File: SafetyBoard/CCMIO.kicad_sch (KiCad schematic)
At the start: 24 parts, among them J13 RTD B, J14 Brakelight, J15 SHOCK/WHEEL SNSR, J16 footwell, J18 AMP, J19 39306207

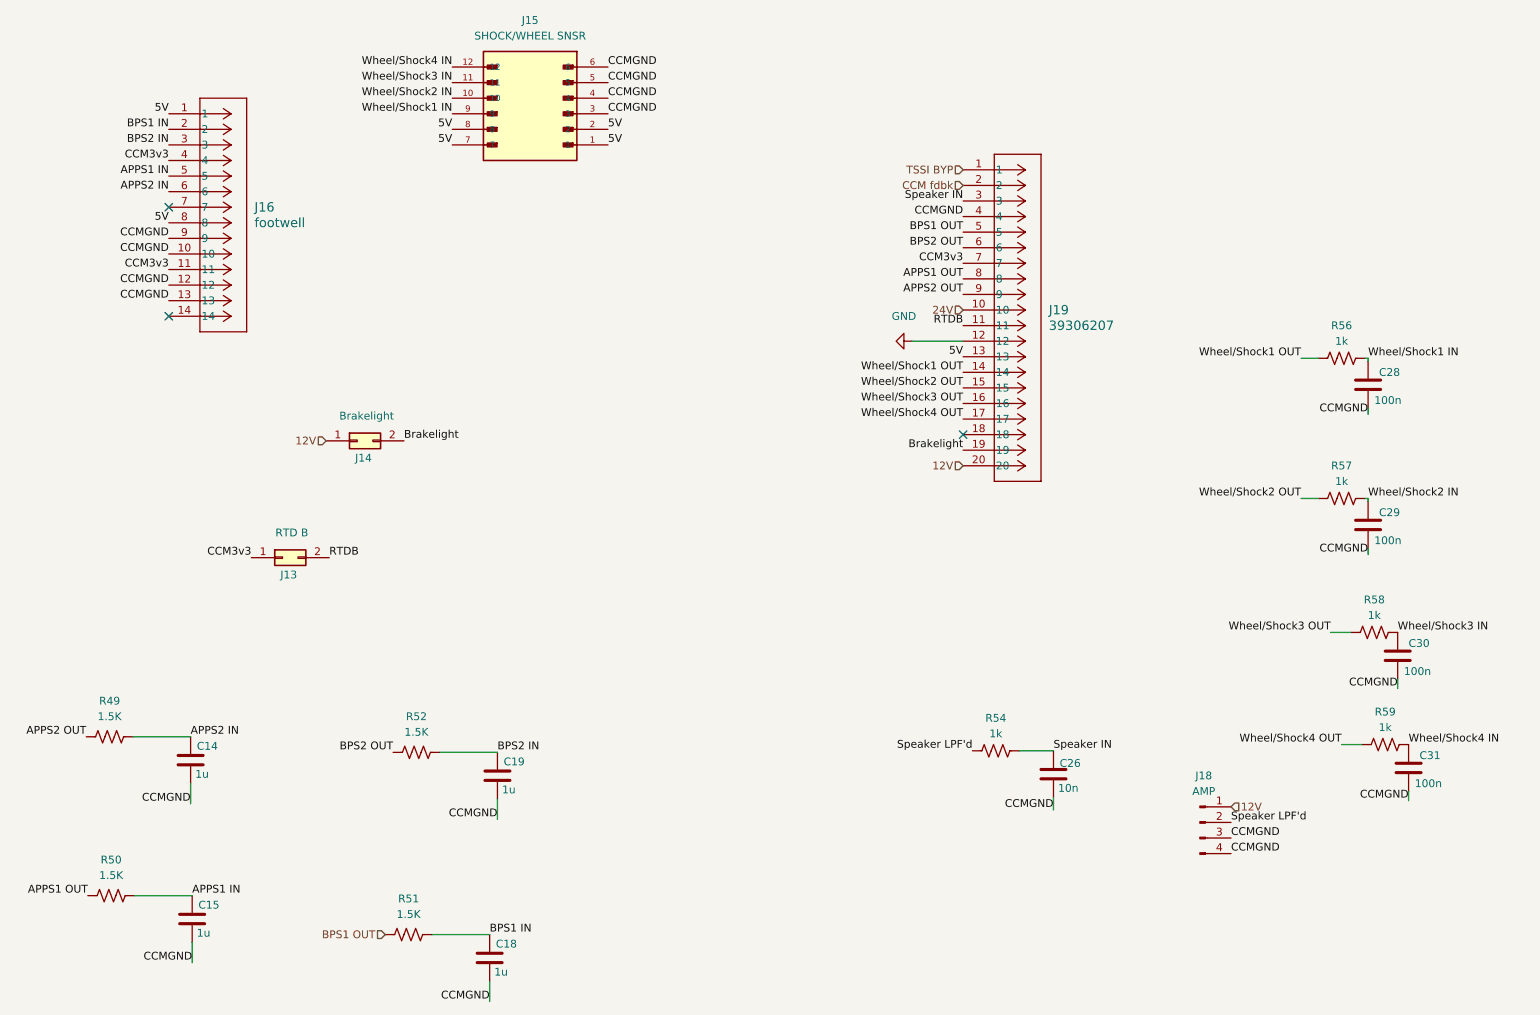
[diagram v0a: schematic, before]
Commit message: I think think this is final but need to defuck the BOM
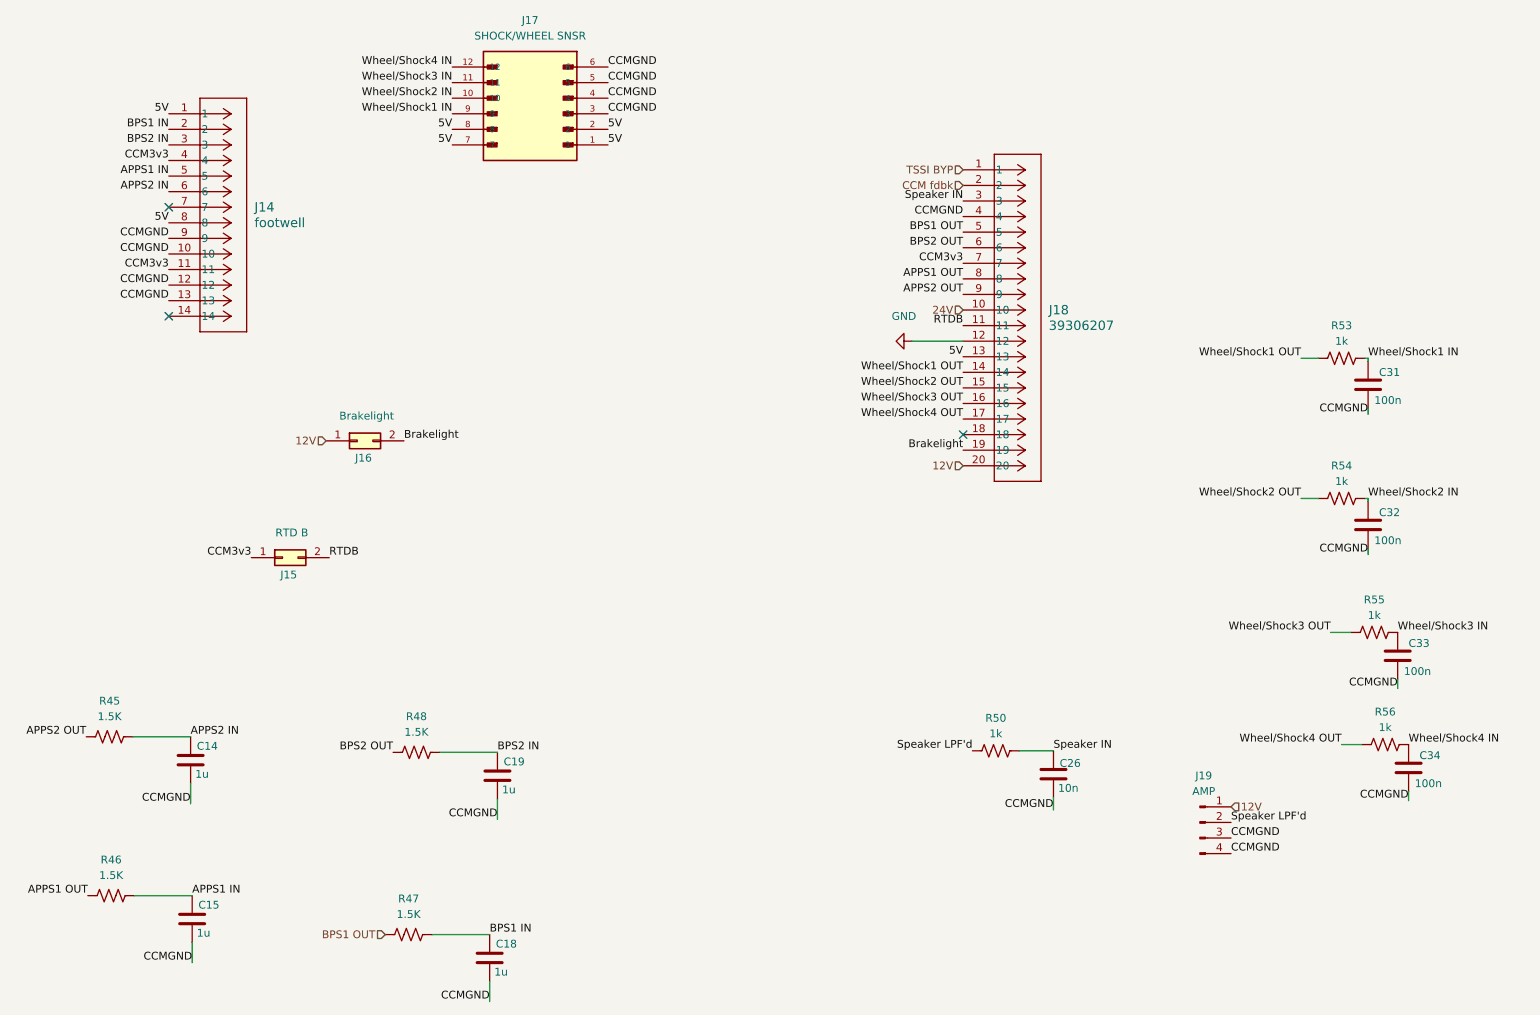
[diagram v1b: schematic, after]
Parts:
- renumbered C28 to C31, C29 to C32, C30 to C33, C31 to C34, J16 to J14, J13 to J15, J14 to J16, J15 to J17, J19 to J18, J18 to J19, R49 to R45, R50 to R46, R51 to R47, R52 to R48, R54 to R50, R56 to R53, R57 to R54, R58 to R55, R59 to R56
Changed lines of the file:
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@@
 		(dnp no)
 		(fields_autoplaced yes)
-		(property "Reference" "R54"
+		(property "Reference" "R50"
 			(at 186.944 141.732 90)
 			(effects
@@
 			(project "SafetyBoard"
 				(path "/30d029c6-868b-41ac-953d-167a7d76c1a3/7a856abf-55a7-4dec-ad85-14c5270a1780"
-					(reference "R54")
+					(reference "R50")
 					(unit 1)
 				)
@@
 		(dnp no)
 		(fields_autoplaced yes)
-		(property "Reference" "R50"
+		(property "Reference" "R46"
 			(at 42.672 164.846 90)
 			(effects
@@
 			(project "SafetyBoard"
 				(path "/30d029c6-868b-41ac-953d-167a7d76c1a3/7a856abf-55a7-4dec-ad85-14c5270a1780"
-					(reference "R50")
+					(reference "R46")
 					(unit 1)
 				)
@@
 		(dnp no)
 		(fields_autoplaced yes)
-		(property "Reference" "R52"
+		(property "Reference" "R48"
 			(at 92.456 141.478 90)
 			(effects
@@
 			(project "SafetyBoard"
 				(path "/30d029c6-868b-41ac-953d-167a7d76c1a3/7a856abf-55a7-4dec-ad85-14c5270a1780"
-					(reference "R52")
+					(reference "R48")
 					(unit 1)
 				)
@@
 		(on_board yes)
 		(dnp no)
-		(property "Reference" "C28"
+		(property "Reference" "C31"
 			(at 249.428 85.344 0)
 			(effects
@@
 			(project "SafetyBoard"
 				(path "/30d029c6-868b-41ac-953d-167a7d76c1a3/7a856abf-55a7-4dec-ad85-14c5270a1780"
-					(reference "C28")
+					(reference "C31")
 					(unit 1)
 				)
@@
 		(dnp no)
 		(fields_autoplaced yes)
-		(property "Reference" "R51"
+		(property "Reference" "R47"
 			(at 91.186 171.196 90)
 			(effects
@@
 			(project "SafetyBoard"
 				(path "/30d029c6-868b-41ac-953d-167a7d76c1a3/7a856abf-55a7-4dec-ad85-14c5270a1780"
-					(reference "R51")
+					(reference "R47")
 					(unit 1)
 				)
@@
 		(dnp no)
 		(fields_autoplaced yes)
-		(property "Reference" "J15"
+		(property "Reference" "J17"
 			(at 110.998 27.94 0)
 			(effects
@@
 			(project "SafetyBoard"
 				(path "/30d029c6-868b-41ac-953d-167a7d76c1a3/7a856abf-55a7-4dec-ad85-14c5270a1780"
-					(reference "J15")
+					(reference "J17")
 					(unit 1)
 				)
@@
 		(on_board yes)
 		(dnp no)
-		(property "Reference" "J14"
+		(property "Reference" "J16"
 			(at 83.82 99.314 0)
 			(effects
@@
 			(project "SafetyBoard"
 				(path "/30d029c6-868b-41ac-953d-167a7d76c1a3/7a856abf-55a7-4dec-ad85-14c5270a1780"
-					(reference "J14")
+					(reference "J16")
 					(unit 1)
 				)
@@
 		(dnp no)
 		(fields_autoplaced yes)
-		(property "Reference" "R57"
+		(property "Reference" "R54"
 			(at 243.332 100.584 90)
 			(effects
@@
 			(project "SafetyBoard"
 				(path "/30d029c6-868b-41ac-953d-167a7d76c1a3/7a856abf-55a7-4dec-ad85-14c5270a1780"
-					(reference "R57")
+					(reference "R54")
 					(unit 1)
 				)
@@
 		(dnp no)
 		(fields_autoplaced yes)
-		(property "Reference" "R58"
+		(property "Reference" "R55"
 			(at 248.666 122.428 90)
 			(effects
@@
 			(project "SafetyBoard"
 				(path "/30d029c6-868b-41ac-953d-167a7d76c1a3/7a856abf-55a7-4dec-ad85-14c5270a1780"
-					(reference "R58")
+					(reference "R55")
 					(unit 1)
 				)
@@
 		(dnp no)
 		(fields_autoplaced yes)
-		(property "Reference" "R59"
+		(property "Reference" "R56"
 			(at 250.444 140.716 90)
 			(effects
@@
 			(project "SafetyBoard"
 				(path "/30d029c6-868b-41ac-953d-167a7d76c1a3/7a856abf-55a7-4dec-ad85-14c5270a1780"
-					(reference "R59")
+					(reference "R56")
 					(unit 1)
 				)
@@
 		(on_board yes)
 		(dnp no)
-		(property "Reference" "C30"
+		(property "Reference" "C33"
 			(at 254.254 129.54 0)
 			(effects
@@
 			(project "SafetyBoard"
 				(path "/30d029c6-868b-41ac-953d-167a7d76c1a3/7a856abf-55a7-4dec-ad85-14c5270a1780"
-					(reference "C30")
+					(reference "C33")
 					(unit 1)
 				)
@@
 		(on_board yes)
 		(dnp no)
-		(property "Reference" "C29"
+		(property "Reference" "C32"
 			(at 249.428 108.204 0)
 			(effects
@@
 			(project "SafetyBoard"
 				(path "/30d029c6-868b-41ac-953d-167a7d76c1a3/7a856abf-55a7-4dec-ad85-14c5270a1780"
-					(reference "C29")
+					(reference "C32")
 					(unit 1)
 				)
@@
 		(on_board yes)
 		(dnp no)
-		(property "Reference" "C31"
+		(property "Reference" "C34"
 			(at 256.032 147.828 0)
 			(effects
@@
 			(project "SafetyBoard"
 				(path "/30d029c6-868b-41ac-953d-167a7d76c1a3/7a856abf-55a7-4dec-ad85-14c5270a1780"
-					(reference "C31")
+					(reference "C34")
 					(unit 1)
 				)
@@
 		(on_board yes)
 		(dnp no)
-		(property "Reference" "J13"
+		(property "Reference" "J15"
 			(at 71.628 118.364 0)
 			(effects
@@
 			(project "SafetyBoard"
 				(path "/30d029c6-868b-41ac-953d-167a7d76c1a3/7a856abf-55a7-4dec-ad85-14c5270a1780"
-					(reference "J13")
+					(reference "J15")
 					(unit 1)
 				)
@@
 		(dnp no)
 		(fields_autoplaced yes)
-		(property "Reference" "J18"
+		(property "Reference" "J19"
 			(at 220.853 151.13 0)
 			(effects
@@
 			(project ""
 				(path "/30d029c6-868b-41ac-953d-167a7d76c1a3/7a856abf-55a7-4dec-ad85-14c5270a1780"
-					(reference "J18")
+					(reference "J19")
 					(unit 1)
 				)
@@
 		(dnp no)
 		(fields_autoplaced yes)
-		(property "Reference" "J19"
+		(property "Reference" "J18"
 			(at 195.58 75.1839 0)
 			(effects
@@
 			(project ""
 				(path "/30d029c6-868b-41ac-953d-167a7d76c1a3/7a856abf-55a7-4dec-ad85-14c5270a1780"
-					(reference "J19")
+					(reference "J18")
 					(unit 1)
 				)
@@
 		(dnp no)
 		(fields_autoplaced yes)
-		(property "Reference" "J16"
+		(property "Reference" "J14"
 			(at 66.04 58.4199 0)
 			(effects
@@
 			(project ""
 				(path "/30d029c6-868b-41ac-953d-167a7d76c1a3/7a856abf-55a7-4dec-ad85-14c5270a1780"
-					(reference "J16")
+					(reference "J14")
 					(unit 1)
 				)
@@
 		(dnp no)
 		(fields_autoplaced yes)
-		(property "Reference" "R49"
+		(property "Reference" "R45"
 			(at 42.418 138.938 90)
 			(effects
@@
 			(project "SafetyBoard"
 				(path "/30d029c6-868b-41ac-953d-167a7d76c1a3/7a856abf-55a7-4dec-ad85-14c5270a1780"
-					(reference "R49")
+					(reference "R45")
 					(unit 1)
 				)
@@
 		(dnp no)
 		(fields_autoplaced yes)
-		(property "Reference" "R56"
+		(property "Reference" "R53"
 			(at 243.332 77.724 90)
 			(effects
@@
 			(project "SafetyBoard"
 				(path "/30d029c6-868b-41ac-953d-167a7d76c1a3/7a856abf-55a7-4dec-ad85-14c5270a1780"
-					(reference "R56")
+					(reference "R53")
 					(unit 1)
 				)
@@
 		(dnp no)
 		(fields_autoplaced yes)
-		(property "Reference" "#PWR095"
+		(property "Reference" "#PWR099"
 			(at 166.878 80.264 0)
 			(effects
@@
 			(project "SafetyBoard"
 				(path "/30d029c6-868b-41ac-953d-167a7d76c1a3/7a856abf-55a7-4dec-ad85-14c5270a1780"
-					(reference "#PWR095")
-					(unit 1)
-				)
+					(reference "#PWR099")
+					(unit 1)
+				)

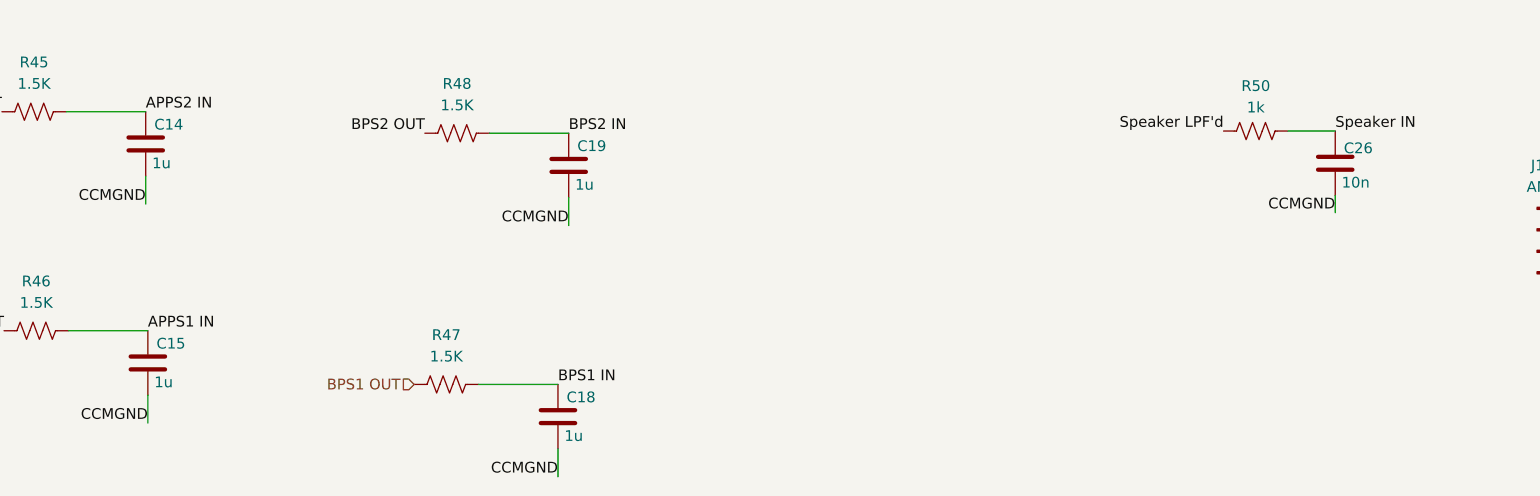
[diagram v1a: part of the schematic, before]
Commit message: Safety Board: added BOM and updated schematics
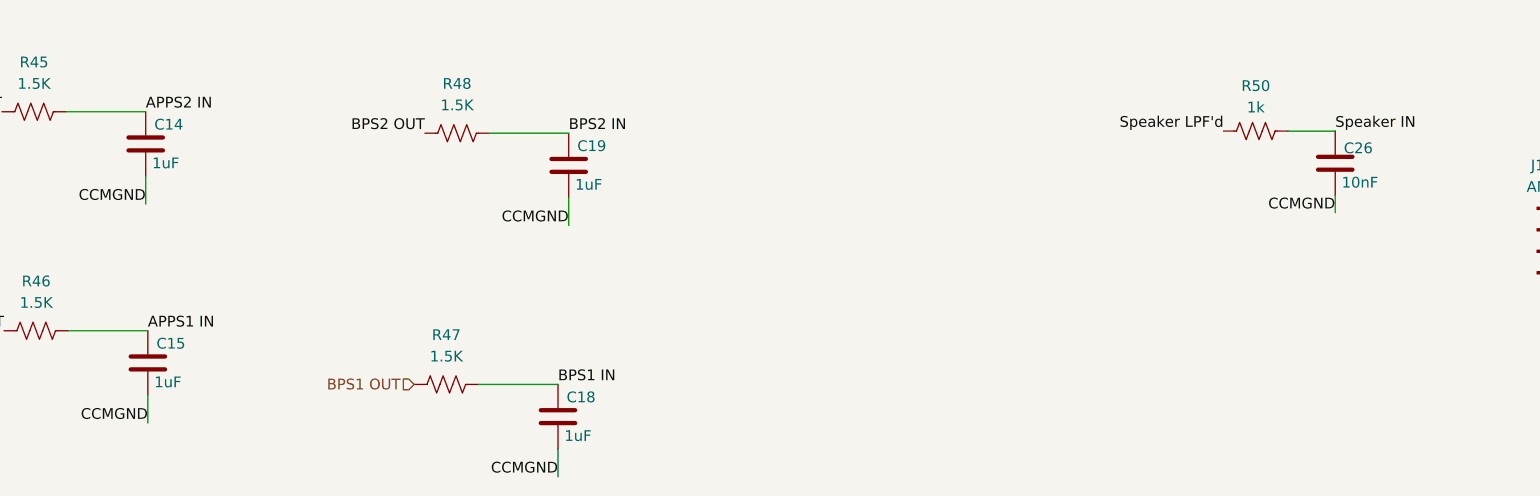
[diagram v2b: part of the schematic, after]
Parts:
- C14, C15, C18, C19: value 1u -> 1uF
- C26: value 10n -> 10nF
- J14: MFG (none) -> Molex; MPN (none) -> 0039281143
- J15, J16: MFG (none) -> Molex; MPN (none) -> 0039310028
- J17: MFG (none) -> Molex; MPN (none) -> 39-30-6127
- J18: MFG (none) -> Molex; MPN (none) -> 39306207
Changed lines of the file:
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@@
 			)
 		)
-		(property "Datasheet" ""
+		(property "Datasheet" "~"
 			(at 186.944 147.066 0)
 			(effects
@@
 			)
 		)
-		(property "Datasheet" "https://www.digikey.com/en/products/detail/panasonic-electronic-components/ERJ-6GEYJ152V/83022"
+		(property "Datasheet" "~"
 			(at 42.672 170.688 0)
 			(effects
@@
 			)
 		)
-		(property "Datasheet" "https://www.digikey.com/en/products/detail/panasonic-electronic-components/ERJ-6GEYJ152V/83022"
+		(property "Datasheet" "~"
 			(at 92.456 147.32 0)
 			(effects
@@
 			)
 		)
-		(property "Datasheet" "https://www.digikey.com/en/products/detail/yageo/CC0805KRX7R9BB104/302874"
+		(property "Datasheet" "~"
 			(at 247.65 87.376 0)
 			(effects
@@
 			)
 		)
-		(property "Datasheet" "https://www.digikey.com/en/products/detail/panasonic-electronic-components/ERJ-6GEYJ152V/83022"
+		(property "Datasheet" "~"
 			(at 91.186 177.038 0)
 			(effects
@@
 			)
 		)
+		(property "MFG" "Molex"
+			(at 110.998 43.18 0)
+			(effects
+				(font
+					(size 1.27 1.27)
+				)
+				(hide yes)
+			)
+		)
+		(property "MPN" "39-30-6127"
+			(at 110.998 43.18 0)
+			(effects
+				(font
+					(size 1.27 1.27)
+				)
+				(hide yes)
+			)
+		)
 		(pin "3"
 		)
@@
 		)
 		(property "Description" "Generic connector, double row, 02x01, this symbol is compatible with counter-clockwise, top-bottom and odd-even numbering schemes., script generated (kicad-library-utils/schlib/autogen/connector/)"
+			(at 82.804 96.52 0)
+			(effects
+				(font
+					(size 1.27 1.27)
+				)
+				(hide yes)
+			)
+		)
+		(property "MFG" "Molex"
+			(at 82.804 96.52 0)
+			(effects
+				(font
+					(size 1.27 1.27)
+				)
+				(hide yes)
+			)
+		)
+		(property "MPN" "0039310028"
 			(at 82.804 96.52 0)
 			(effects
@@
 			)
 		)
-		(property "Datasheet" ""
+		(property "Datasheet" "~"
 			(at 243.332 105.918 0)
 			(effects
@@
 			)
 		)
-		(property "Datasheet" ""
+		(property "Datasheet" "~"
 			(at 248.666 127.762 0)
 			(effects
@@
 			)
 		)
-		(property "Datasheet" ""
+		(property "Datasheet" "~"
 			(at 250.444 146.05 0)
 			(effects
@@
 			)
 		)
-		(property "Datasheet" "https://www.digikey.com/en/products/detail/yageo/CC0805KRX7R9BB104/302874"
+		(property "Datasheet" "~"
 			(at 252.476 131.572 0)
 			(effects
@@
 			)
 		)
-		(property "Value" "1u"
+		(property "Value" "1uF"
 			(at 105.156 183.134 0)
 			(effects
@@
 			)
 		)
-		(property "Datasheet" "https://www.digikey.com/en/products/detail/samsung-electro-mechanics/CL21B105KBFNNNE/3886687"
+		(property "Datasheet" "~"
 			(at 104.394 180.848 0)
 			(effects
@@
 			)
 		)
-		(property "Value" "10n"
+		(property "Value" "10nF"
 			(at 197.104 153.162 0)
 			(do_not_autoplace yes)
@@
 			)
 		)
-		(property "Datasheet" "https://www.digikey.com/en/products/detail/samsung-electro-mechanics/CL21B103KBANNNC/3886673"
+		(property "Datasheet" "~"
 			(at 196.342 150.876 0)
 			(effects
@@
 			)
 		)
-		(property "Datasheet" "https://www.digikey.com/en/products/detail/yageo/CC0805KRX7R9BB104/302874"
+		(property "Datasheet" "~"
 			(at 247.65 110.236 0)
 			(effects
@@
 			)
 		)
-		(property "Datasheet" "https://www.digikey.com/en/products/detail/yageo/CC0805KRX7R9BB104/302874"
+		(property "Datasheet" "~"
 			(at 254.254 149.86 0)
 			(effects
@@
 			)
 		)
-		(property "Value" "1u"
+		(property "Value" "1uF"
 			(at 56.642 176.784 0)
 			(effects
@@
 			)
 		)
-		(property "Datasheet" "https://www.digikey.com/en/products/detail/samsung-electro-mechanics/CL21B105KBFNNNE/3886687"
+		(property "Datasheet" "~"
 			(at 55.88 174.498 0)
 			(effects
@@
 			)
 		)
-		(property "Value" "1u"
+		(property "Value" "1uF"
 			(at 56.388 150.876 0)
 			(effects
@@
 			)
 		)
-		(property "Datasheet" "https://www.digikey.com/en/products/detail/samsung-electro-mechanics/CL21B105KBFNNNE/3886687"
+		(property "Datasheet" "~"
 			(at 55.626 148.59 0)
 			(effects
@@
 		)
 		(property "Description" "Generic connector, double row, 02x01, this symbol is compatible with counter-clockwise, top-bottom and odd-even numbering schemes., script generated (kicad-library-utils/schlib/autogen/connector/)"
+			(at 70.612 115.57 0)
+			(effects
+				(font
+					(size 1.27 1.27)
+				)
+				(hide yes)
+			)
+		)
+		(property "MFG" "Molex"
+			(at 70.612 115.57 0)
+			(effects
+				(font
+					(size 1.27 1.27)
+				)
+				(hide yes)
+			)
+		)
+		(property "MPN" "0039310028"
 			(at 70.612 115.57 0)
 			(effects
@@
 			)
 		)
+		(property "MFG" "Molex"
+			(at 181.61 52.324 0)
+			(effects
+				(font
+					(size 1.27 1.27)
+				)
+				(hide yes)
+			)
+		)
+		(property "MPN" "39306207"
+			(at 181.61 52.324 0)
+			(effects
+				(font
+					(size 1.27 1.27)
+				)
+				(hide yes)
+			)
+		)
 		(pin "15"
 		)
@@
 			)
 		)
+		(property "MFG" "Molex "
+			(at 52.07 43.18 0)
+			(effects
+				(font
+					(size 1.27 1.27)
+				)
+				(hide yes)
+			)
+		)
+		(property "MPN" "0039281143"
+			(at 52.07 43.18 0)
+			(effects
+				(font
+					(size 1.27 1.27)
+				)
+				(hide yes)
+			)
+		)
 		(pin "3"
 		)
@@
 			)
 		)
-		(property "Value" "1u"
+		(property "Value" "1uF"
 			(at 106.426 153.416 0)
 			(effects
@@
 			)
 		)
-		(property "Datasheet" "https://www.digikey.com/en/products/detail/samsung-electro-mechanics/CL21B105KBFNNNE/3886687"
+		(property "Datasheet" "~"
 			(at 105.664 151.13 0)
 			(effects
@@
 			)
 		)
-		(property "Datasheet" "https://www.digikey.com/en/products/detail/panasonic-electronic-components/ERJ-6GEYJ152V/83022"
+		(property "Datasheet" "~"
 			(at 42.418 144.78 0)
 			(effects
@@
 			)
 		)
-		(property "Datasheet" ""
+		(property "Datasheet" "~"
 			(at 243.332 83.058 0)
 			(effects
